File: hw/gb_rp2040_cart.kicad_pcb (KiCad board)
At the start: 2 copper layers, 51.4 x 60.5 mm, 53 parts, among them J1 GameBoy_Cartridge, J2 USB_C_Receptacle_USB2.0, J3 USB_BOOT, J4 DEBUG, Q1 Si2319CDS, SW1 RST, U1 SN74AUP1T34DCK, U10 RP2040, U11 FAN53600, U2 SN74AUP1T34DCK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

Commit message: hw: finish layout
Signed-off-by: Mahyar Koshkouei <mk@deltabeard.com>
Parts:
- removed U2, U6, U7: SN74AUP1T34DCK, Package_TO_SOT_SMD:SOT-353_SC-70-5
- removed U3, U4, U5: 74LVC8T245PW, Package_SO:TSSOP-24_4.4x7.8mm_P0.65mm
- added C19: 100n, Capacitor_SMD:C_0603_1608Metric, F.Cu at (64.8, 112.7)
- added C20: 100n, Capacitor_SMD:C_0603_1608Metric, F.Cu at (81.0, 114.8)
- added C21: 100n, Capacitor_SMD:C_0603_1608Metric, F.Cu at (55.9, 109.9)
- added C22: 100n, Capacitor_SMD:C_0603_1608Metric, F.Cu at (58.9, 102.1)
- added C23: 100n, Capacitor_SMD:C_0603_1608Metric, F.Cu at (94.5, 102.5)
- added C24: 100n, Capacitor_SMD:C_0603_1608Metric, F.Cu at (89.2, 114.8)
- added C25: 100n, Capacitor_SMD:C_0603_1608Metric, F.Cu at (64.8, 109.5)
- added C26: 100n, Capacitor_SMD:C_0603_1608Metric, F.Cu at (81.0, 111.5)
- added C27: 100n, Capacitor_SMD:C_0603_1608Metric, F.Cu at (89.2, 111.5)
- added IC1: CLXC8T245QRHLRQ1, Project_Specific:CLXC8T245QRHLRQ1, F.Cu at (93.2, 114.0)
- added IC2: CLXC8T245QRHLRQ1, Project_Specific:CLXC8T245QRHLRQ1, F.Cu at (85.2, 114.0)
- added IC3: CLXC8T245QRHLRQ1, Project_Specific:CLXC8T245QRHLRQ1, F.Cu at (69.0, 112.0)
- added J5: Expansion, Connector_PinSocket_2.54mm:PinSocket_1x04_P2.54mm_Horizontal, F.Cu at (83.2, 81.3)
- added Q2: RU1J002YN, Package_TO_SOT_SMD:SOT-323_SC-70, F.Cu at (94.0, 106.0)
- added TP2: MFP, TestPoint:TestPoint_Pad_D1.0mm, F.Cu at (98.5, 109.2)
- added TP3: MFP, TestPoint:TestPoint_Pad_D1.0mm, F.Cu at (100.5, 109.2)
- added TP4: MFP, TestPoint:TestPoint_Pad_D1.0mm, F.Cu at (100.2, 95.8)
- added U12: PCA9536D, Package_SO:SOIC-8_3.9x4.9mm_P1.27mm, F.Cu at (98.4, 104.0)
- C15, C7, U9: moved to B.Cu
- J2: value USB_C_Receptacle_USB2.0 -> USB4105-GF-A; footprint Connector_USB:USB_C_Receptacle_XKB_U262-16XN-4BVC11 -> Project_Specific:GCT_USB4105-GF-A
- R3: value 600R -> 1k
- TP1: footprint TestPoint:TestPoint_THTPad_D2.0mm_Drill1.0mm -> TestPoint:TestPoint_Pad_D1.5mm
- U1: value SN74AUP1T34DCK -> TXU0104; footprint Package_TO_SOT_SMD:SOT-353_SC-70-5 -> Package_SO:TSSOP-14_4.4x5mm_P0.65mm
- moved TP1 99.7 mm to (55.1, 90.9), turned to 180 degrees
- moved BT1 90.5 mm to (58.4, 86.9)
- moved C1 88.4 mm to (58.5, 92.9), turned to 180 degrees
- moved U8 87.8 mm to (59.1, 90.7), turned to 180 degrees
- moved Q1 87.2 mm to (53.8, 118.6), turned to 180 degrees
- moved R9 84.7 mm to (55.5, 121.1)
- moved C16 82.7 mm to (54.2, 116.0), turned to 180 degrees
- moved D1 82.4 mm to (66.1, 86.1), turned to 90 degrees
- moved R3 81.1 mm to (63.3, 86.7), turned to 180 degrees
- moved D2 80.2 mm to (56.7, 118.5), turned to -90 degrees
- moved C18 79.9 mm to (55.7, 113.7), turned to 180 degrees
- moved Y1 79.9 mm to (63.3, 91.3), turned to 90 degrees
- moved SW1 79.2 mm to (76.0, 110.0), turned to -90 degrees
- moved U11 78.0 mm to (56.7, 115.8), turned to 90 degrees
- moved L1 76.3 mm to (58.5, 114.7), turned to 90 degrees
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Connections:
- J1 pad 30: unconnected-(J1-Pad30) -> ~{RES}
- U1 pad 3: GND -> ~{WR}
- U1 pad 4: PHI_3V3 -> ~{RD}
- U1 pad 5: +3V3 -> (no net)
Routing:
- net +3V3: track 0.00 -> 39.0 mm, vias 0 -> 2
- net /A7: track 0.00 -> 21.2 mm
- net /A15: track 0.00 -> 21.2 mm
- net /A10: track 0.00 -> 21.2 mm
- net /A1: track 0.00 -> 21.0 mm
- net /A3: track 0.00 -> 21.0 mm
- net /A5: track 0.00 -> 20.9 mm
- net /A6: track 0.00 -> 20.8 mm
- net PHI: track 0.00 -> 20.2 mm
- net ~{WR}: track 0.00 -> 19.9 mm
- net ~{RD}: track 0.00 -> 19.9 mm
- net /A8: track 0.00 -> 19.2 mm
- net /A12: track 0.00 -> 19.1 mm
- net /A0: track 0.00 -> 19.1 mm
- net /A14: track 0.00 -> 19.1 mm
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- added copper zone on F.Cu, net +3V3
- added copper zone on F.Cu, net +5V
- added copper zone on F.Cu, net GND
- added copper zone on F.Cu, net Net-(L1-Pad1)

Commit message: Finish routing & final checks
Signed-off-by: Mahyar Koshkouei <mk@deltabeard.com>
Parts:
- removed D2: D_Schottky, Diode_SMD:D_0603_1608Metric
- removed Q1: Si2319CDS, Package_TO_SOT_SMD:SOT-23
- added C28: 100n, Capacitor_SMD:C_0603_1608Metric, F.Cu at (55.0, 107.3)
- added C29: 100n, Capacitor_SMD:C_0603_1608Metric, F.Cu at (55.8, 101.1)
- added R12: 1k, Resistor_SMD:R_0603_1608Metric, F.Cu at (60.2, 101.1)
- added U2: TPS2115, Package_SO:TSSOP-8_4.4x3mm_P0.65mm, F.Cu at (58.0, 103.7)
- C23, Q2, R10, R11, R2, R4, TP2, TP3, TP4, U12: moved to B.Cu
- R9: value 10k -> 1k
- moved R9 22.1 mm to (60.2, 99.5)
- moved TP4 18.9 mm to (88.4, 110.5)
- moved C18 17.8 mm to (56.8, 95.8)
- moved L1 17.8 mm to (59.6, 96.8)
- moved C16 17.8 mm to (55.3, 98.2)
- moved U11 17.8 mm to (57.8, 98.0)
- moved C22 16.7 mm to (75.0, 106.4), turned to 180 degrees
- moved C21 14.6 mm to (66.5, 99.9), turned to 90 degrees
- moved TP3 13.7 mm to (90.2, 118.2)
- moved R11 12.6 mm to (90.9, 108.2), turned to 0 degrees
- moved TP2 11.0 mm to (92.2, 118.2)
- moved U12 10.9 mm to (92.3, 113.0)
- moved U1 9.45 mm to (69.4, 104.4), turned to 0 degrees
- moved R10 9.44 mm to (93.9, 108.2), turned to 180 degrees
- moved Q2 9.38 mm to (96.7, 115.0)
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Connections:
- net /USB_DM renamed /USB_DN
- R9 pad 1: VBUS -> GND
- R9 pad 2: GND -> Net-(R12-Pad2)
- U1 pad 10: PHI_3V3 -> ~{CS}_3V3
- U1 pad 11: +3V3 -> ~{RD}_3V3
- U1 pad 12: +3V3 -> ~{WR}_3V3
- U1 pad 13: (no net) -> PHI_3V3
- U1 pad 14: (no net) -> +3V3
- U1 pad 5: (no net) -> ~{CS}
- U1 pad 6: GND -> (no net)
- U1 pad 7: ~{CS}_3V3 -> GND
- U1 pad 8: ~{RD}_3V3 -> +3V3
- U1 pad 9: ~{WR}_3V3 -> (no net)
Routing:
- net +3V3: track 39.0 -> 185.8 mm, vias 2 -> 10
- net +5V: track 13.4 -> 97.1 mm, vias 0 -> 6
- net VBUS: track 2.13 -> 80.0 mm
- net I2C_SDA: track 0.00 -> 67.3 mm, vias 0 -> 3
- net I2C_SCL: track 0.00 -> 63.0 mm, vias 0 -> 3
- net ~{RD}: track 19.9 -> 65.4 mm, vias 0 -> 2
- net /3V3_D7: track 0.00 -> 39.2 mm
- net /3V3_D6: track 0.00 -> 38.1 mm
- net /3V3_D5: track 0.00 -> 37.1 mm
- net /3V3_D4: track 0.00 -> 36.1 mm
- net /3V3_D3: track 0.00 -> 35.0 mm
- net /3V3_D2: track 0.00 -> 33.9 mm
- net /3V3_D1: track 0.00 -> 32.9 mm
- net GND: track 0.00 -> 31.9 mm, vias 0 -> 62
- net /3V3_A0: track 0.00 -> 31.9 mm
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- added copper zone on B.Cu, net GND
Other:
- board text added: "3V3"
- board text added: "BACK"
- board text added: "Compatible with DMG, MGB, & CGB Revision 0.1a git.io/JEM5x"
- board text added: "DEBUG"
- board text added: "EXPANSION"
- board text added: "GB RP2040 CART"
- board text added: "GND"
- board text added: "JLCJLCJLCJLC"
- board text added: "Mahyar Koshkouei All Rights Reserved"
- board text added: "RP2040"
- board text added: "RST"
- board text added: "RTC"
- board text added: "SCL"
- board text added: "SDA"
- board text added: "SWCLK"
- board text added: "SWDIO"
- board text added: "USB"
- board text added: "USB BOOT"

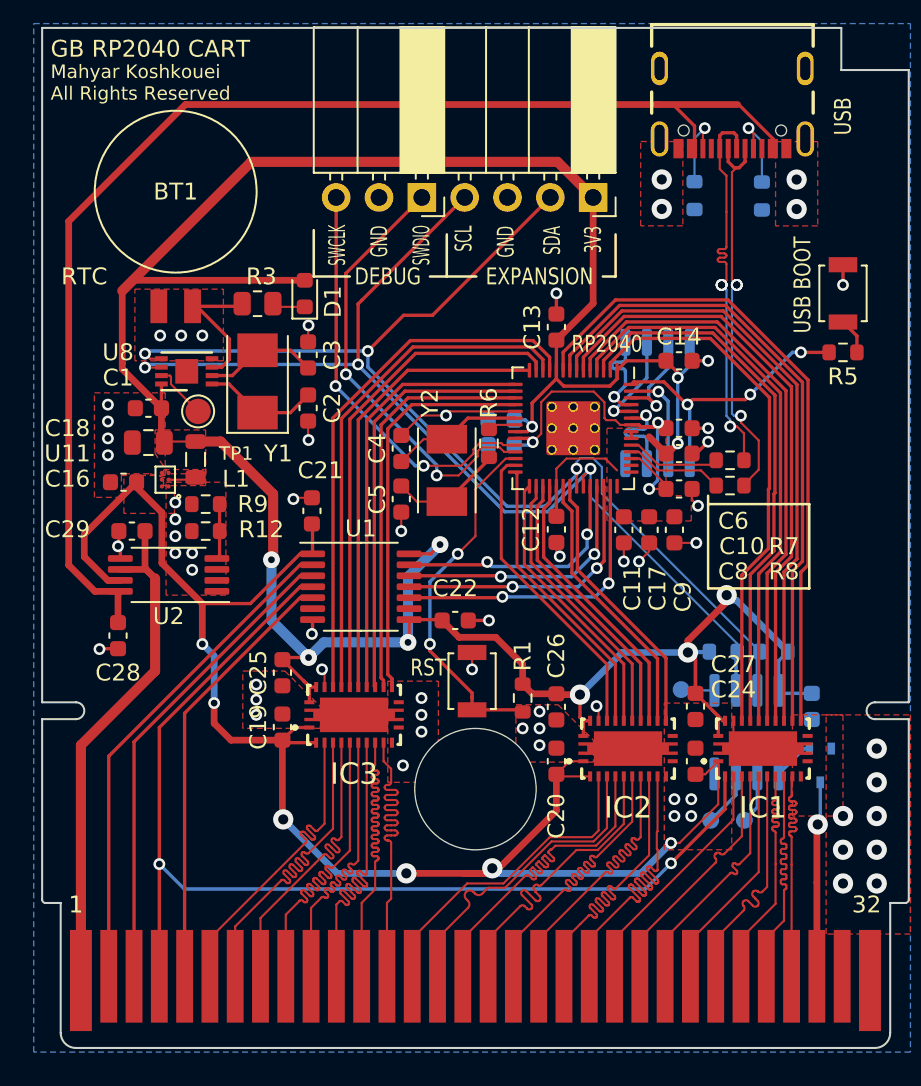
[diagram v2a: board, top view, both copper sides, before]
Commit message: hw: add fix for data direction
Signed-off-by: Mahyar Koshkouei <mk@deltabeard.com>
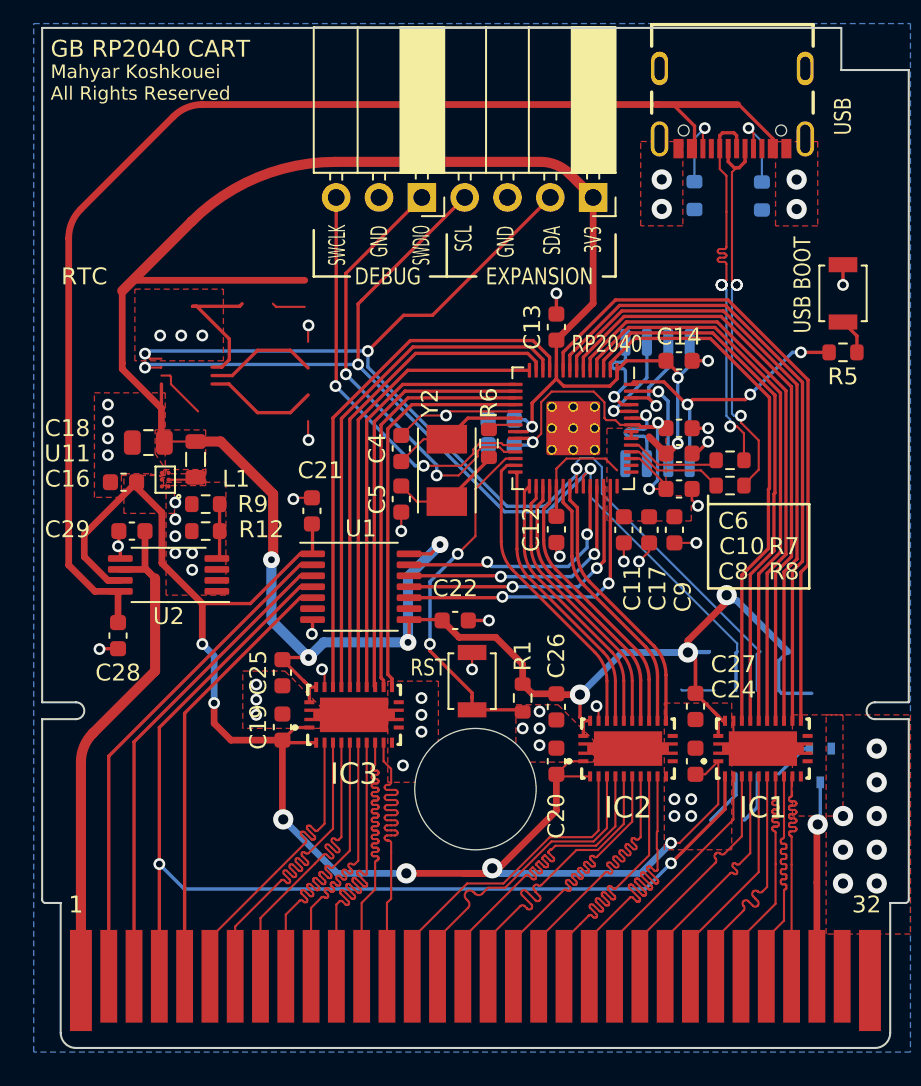
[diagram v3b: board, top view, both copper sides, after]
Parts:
- removed BT1: MS920SE, Project_Specific:BatteryHolder_Seiko_MS920SE
- removed C1, C23: 100n, Capacitor_SMD:C_0603_1608Metric
- removed C2, C3: 8p, Capacitor_SMD:C_0603_1608Metric
- removed D1: D_Schottky, Diode_SMD:D_0603_1608Metric
- removed R10, R11: 5k1, Resistor_SMD:R_0603_1608Metric
- removed R3: 1k, Resistor_SMD:R_0805_2012Metric
- removed TP1: MFP, TestPoint:TestPoint_Pad_D1.5mm
- removed TP2, TP3, TP4: MFP, TestPoint:TestPoint_Pad_D1.0mm
- removed U12: PCA9536D, Package_SO:SOIC-8_3.9x4.9mm_P1.27mm
- removed U8: MCP7940N-xMNY, Package_DFN_QFN:DFN-8-1EP_3x2mm_P0.5mm_EP1.36x1.46mm
- removed Y1: 32.768k, Crystal:Crystal_SMD_5032-2Pin_5.0x3.2mm
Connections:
- IC1 pad 2: ~{RD} -> DATA_DIR
- Q2 pad 1: /RESET_GB -> RESET_GB
- U10 pad 36: I2C_SDA -> RESET_GB
- U10 pad 37: I2C_SCL -> DATA_DIR
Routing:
- net (no net): track 0.00 -> 35.7 mm
- net /VBAT: track 8.42 -> 0.00 mm
- net Net-(C2-Pad1): track 6.84 -> 0.00 mm
- net Net-(C3-Pad2): track 6.76 -> 0.00 mm
- net Net-(TP3-Pad1): track 3.37 -> 0.00 mm
- net Net-(TP1-Pad1): track 3.32 -> 0.00 mm
- net Net-(TP2-Pad1): track 3.07 -> 0.00 mm
- net RESET_GB: track 0.00 -> 2.43 mm
- net /RESET_GB: track 2.43 -> 0.00 mm
- net Net-(TP4-Pad1): track 2.00 -> 0.00 mm
- net Net-(D1-Pad1): track 1.97 -> 0.00 mm
- net +3V3: track 185.8 -> 185.1 mm
